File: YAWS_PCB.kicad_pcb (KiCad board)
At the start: 2 copper layers, 120 x 40 mm, 35 parts, among them J1 Conn_01x02_Male, J3 Conn_02x03_Odd_Even, J4 Conn_01x03, J5 Conn_01x02_Male, J6 Conn_01x02_Male, J7 Conn_01x04, Q1 BSS138, Q2 BSS138, U1 TP4056, U2 LT1763-3.3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

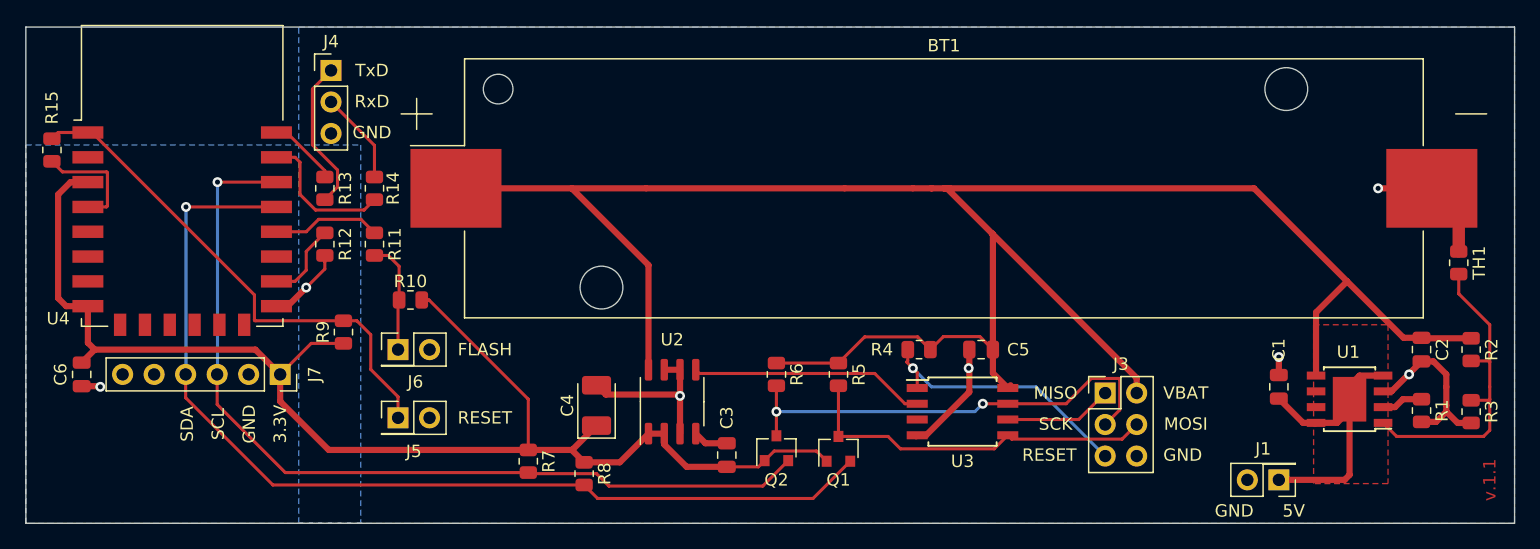
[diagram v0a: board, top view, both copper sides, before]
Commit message: added MOSFET to disconnect TP4056 from battery
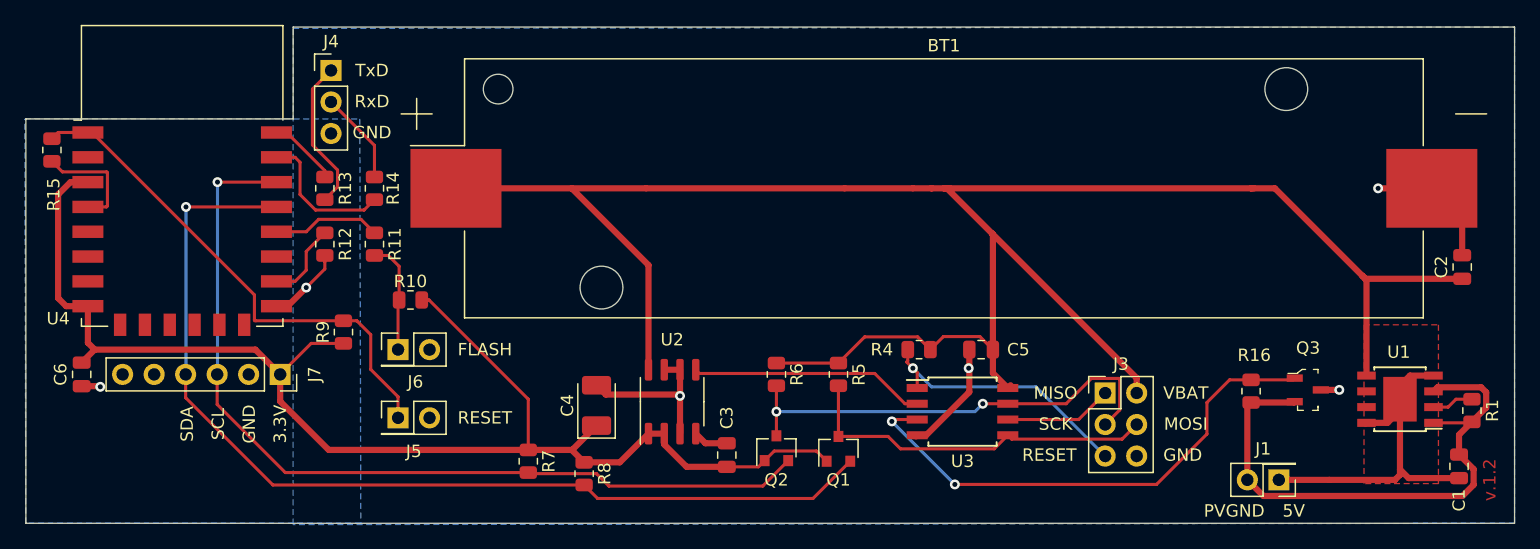
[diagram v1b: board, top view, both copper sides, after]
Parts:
- removed R2: 4.7k, Resistor_SMD:R_0805_2012Metric
- removed R3: 62k, Resistor_SMD:R_0805_2012Metric
- removed TH1: NTC 10k, Resistor_SMD:R_0805_2012Metric
- added Q3: IRLML6344TRPBF, digikey-footprints:SOT-23-3, F.Cu at (243.3, 79.2)
- added R16: 10k, Resistor_SMD:R_0805_2012Metric, F.Cu at (238.8, 79.4)
- moved C1 15.9 mm to (255.5, 85.4)
- moved C2 7.42 mm to (255.8, 69.3), turned to 90 degrees
- moved R1 4.06 mm to (256.6, 80.9)
- moved U1 4.06 mm to (250.8, 80.0)
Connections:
- C1 pad 2: GND -> Net-(C1-Pad2)
- J1 pad 2: GND -> Net-(C1-Pad2)
- R1 pad 2: GND -> Net-(C1-Pad2)
- U1 pad 1: Net-(R2-Pad2) -> Net-(C1-Pad2)
- U1 pad 3: GND -> Net-(C1-Pad2)
- U3 pad 3: Net-(U3-Pad3) -> 5VEN
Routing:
- net Net-(C1-Pad2): track 0.00 -> 46.0 mm
- net 5VEN: track 0.00 -> 41.8 mm, vias 0 -> 2
- net Net-(R2-Pad2): track 26.0 -> 0.00 mm
- net GND: track 58.2 -> 44.4 mm, vias 7 -> 6
- net Net-(C1-Pad1): track 25.1 -> 30.4 mm
- net +BATT: track 168.8 -> 165.9 mm
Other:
- outline, holes or cut-outs redrawn
- board text added: "PVGND"
- board text added: "v.1.2"
- board text removed: "v.1.1"

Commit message: reduced I2C pullups
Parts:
- R5, R6, R7, R8: value 10k -> 4.7k
